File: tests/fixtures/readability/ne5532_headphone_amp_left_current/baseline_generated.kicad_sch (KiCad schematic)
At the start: 13 parts, among them J1 AudioIn_L, J2 AudioIn_R, J3 PowerSupply, J4 HeadphoneOut_L, J5 HeadphoneOut_R

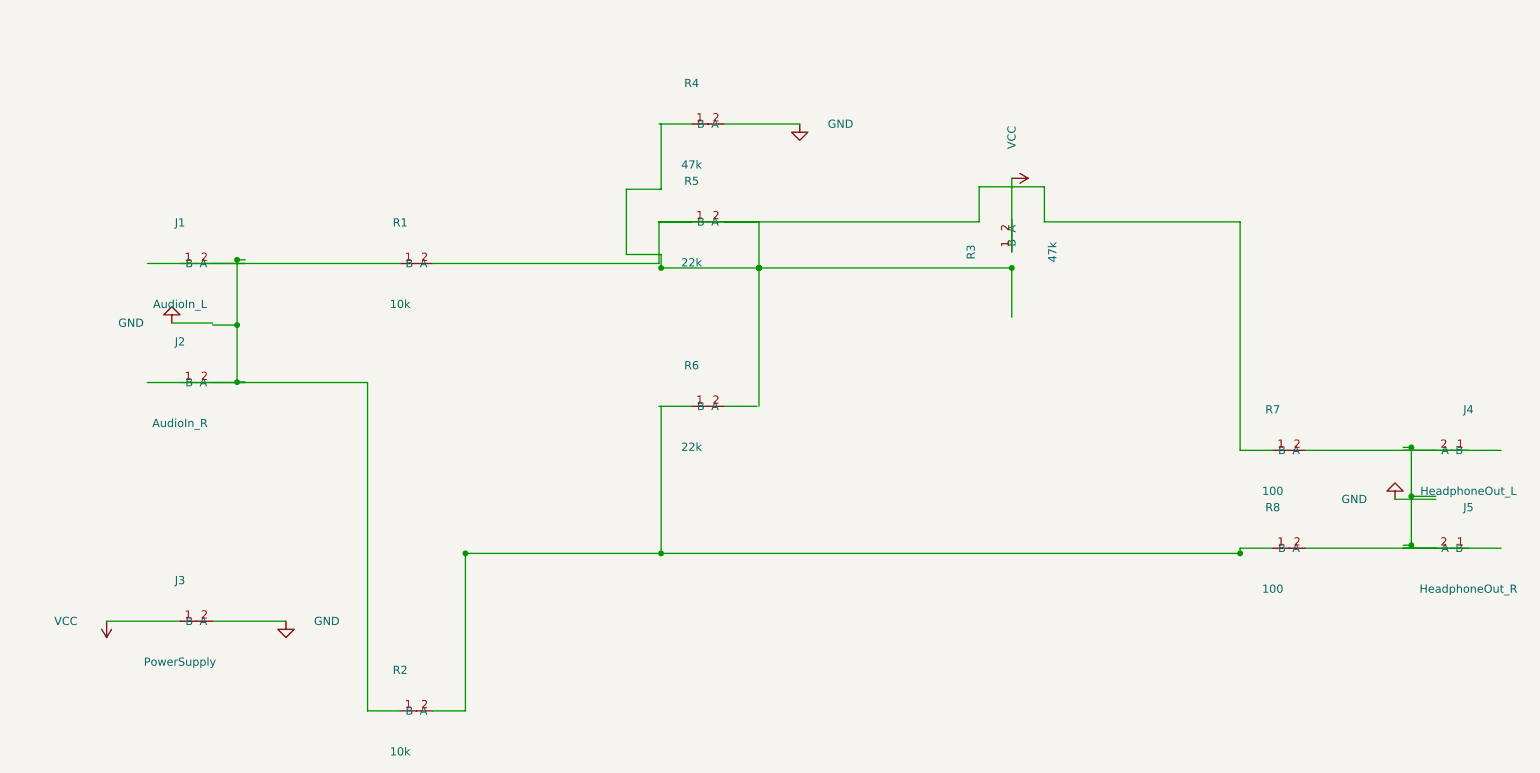
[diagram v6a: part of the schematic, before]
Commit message: fix: correct gnd symbol orientation
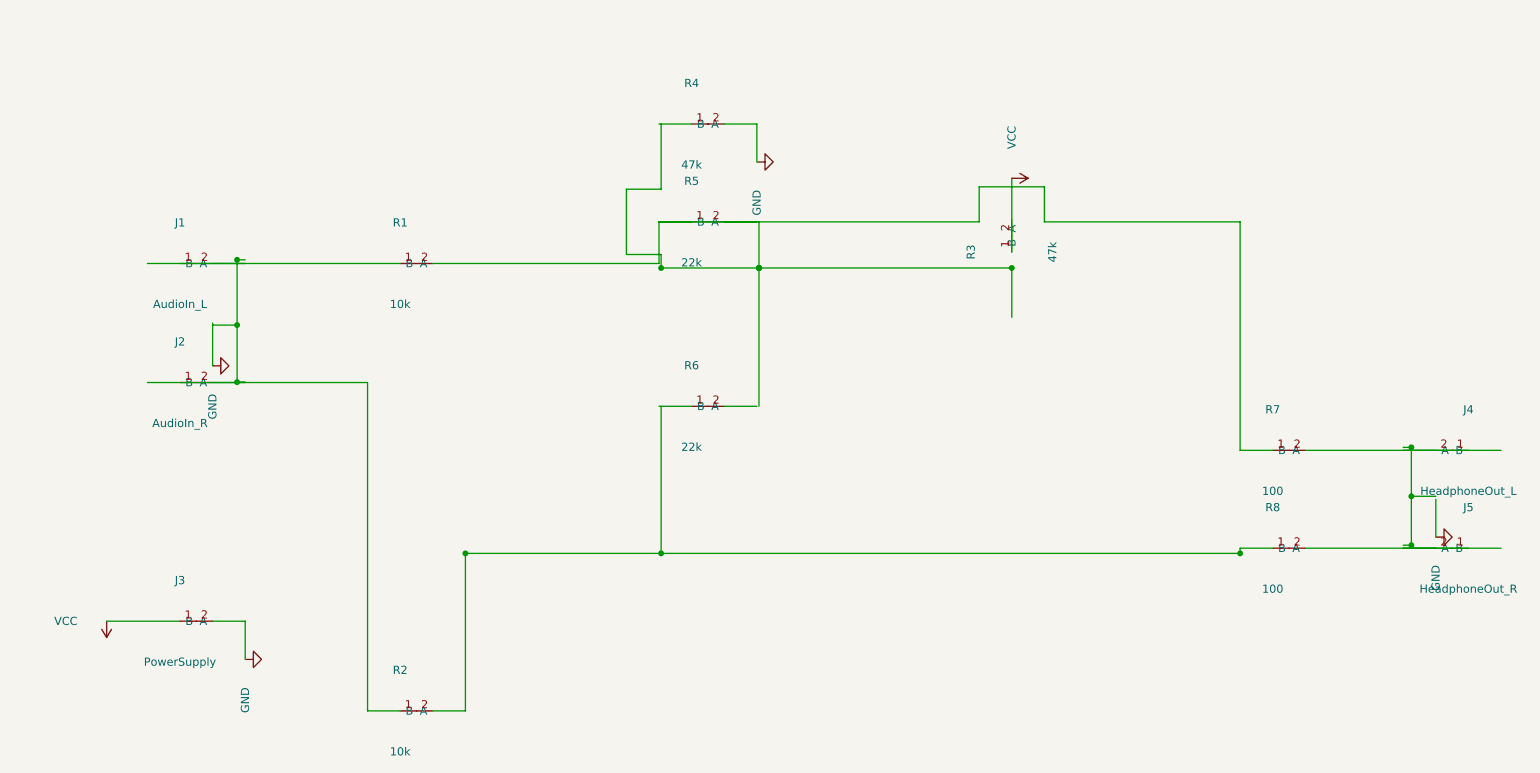
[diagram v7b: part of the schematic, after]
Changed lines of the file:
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@@
         "BaselineHeadphoneAmp"
         (path
-          "/0432db1b-1d3c-47e6-aa61-f27fe61c2f52/"
+          "/7582036d-d91e-40de-9a75-0636ee5f7de5/"
           (reference "J1")
           (unit 1)
@@
         "BaselineHeadphoneAmp"
         (path
-          "/0432db1b-1d3c-47e6-aa61-f27fe61c2f52/"
+          "/7582036d-d91e-40de-9a75-0636ee5f7de5/"
           (reference "J2")
           (unit 1)
@@
         "BaselineHeadphoneAmp"
         (path
-          "/0432db1b-1d3c-47e6-aa61-f27fe61c2f52/"
+          "/7582036d-d91e-40de-9a75-0636ee5f7de5/"
           (reference "J3")
           (unit 1)
@@
         "BaselineHeadphoneAmp"
         (path
-          "/0432db1b-1d3c-47e6-aa61-f27fe61c2f52/"
+          "/7582036d-d91e-40de-9a75-0636ee5f7de5/"
           (reference "J4")
           (unit 1)
@@
         "BaselineHeadphoneAmp"
         (path
-          "/0432db1b-1d3c-47e6-aa61-f27fe61c2f52/"
+          "/7582036d-d91e-40de-9a75-0636ee5f7de5/"
           (reference "J5")
           (unit 1)
@@
         "BaselineHeadphoneAmp"
         (path
-          "/0432db1b-1d3c-47e6-aa61-f27fe61c2f52/"
+          "/7582036d-d91e-40de-9a75-0636ee5f7de5/"
           (reference "R1")
           (unit 1)
@@
         "BaselineHeadphoneAmp"
         (path
-          "/0432db1b-1d3c-47e6-aa61-f27fe61c2f52/"
+          "/7582036d-d91e-40de-9a75-0636ee5f7de5/"
           (reference "R2")
           (unit 1)
@@
         "BaselineHeadphoneAmp"
         (path
-          "/0432db1b-1d3c-47e6-aa61-f27fe61c2f52/"
+          "/7582036d-d91e-40de-9a75-0636ee5f7de5/"
           (reference "R3")
           (unit 1)
@@
         "BaselineHeadphoneAmp"
         (path
-          "/0432db1b-1d3c-47e6-aa61-f27fe61c2f52/"
+          "/7582036d-d91e-40de-9a75-0636ee5f7de5/"
           (reference "R4")
           (unit 1)
@@
         "BaselineHeadphoneAmp"
         (path
-          "/0432db1b-1d3c-47e6-aa61-f27fe61c2f52/"
+          "/7582036d-d91e-40de-9a75-0636ee5f7de5/"
           (reference "R5")
           (unit 1)
@@
         "BaselineHeadphoneAmp"
         (path
-          "/0432db1b-1d3c-47e6-aa61-f27fe61c2f52/"
+          "/7582036d-d91e-40de-9a75-0636ee5f7de5/"
           (reference "R6")
           (unit 1)
@@
         "BaselineHeadphoneAmp"
         (path
-          "/0432db1b-1d3c-47e6-aa61-f27fe61c2f52/"
+          "/7582036d-d91e-40de-9a75-0636ee5f7de5/"
           (reference "R7")
           (unit 1)
@@
         "BaselineHeadphoneAmp"
         (path
-          "/0432db1b-1d3c-47e6-aa61-f27fe61c2f52/"
+          "/7582036d-d91e-40de-9a75-0636ee5f7de5/"
           (reference "R8")
           (unit 1)
@@
   )
   (wire
-    (pts (xy 55.88 108.90) (xy 49.53 108.90))
-    (stroke (width 0) (type default))
-  )
-  (wire
-    (pts (xy 55.88 155.34) (xy 67.31 155.34))
+    (pts (xy 55.88 108.90) (xy 55.88 115.57))
+    (stroke (width 0) (type default))
+  )
+  (wire
+    (pts (xy 55.88 155.34) (xy 60.96 155.34))
+    (stroke (width 0) (type default))
+  )
+  (wire
+    (pts (xy 60.96 155.34) (xy 60.96 161.29))
     (stroke (width 0) (type default))
   )
@@
   )
   (wire
-    (pts (xy 246.38 136.35) (xy 240.03 136.35))
-    (stroke (width 0) (type default))
-  )
-  (wire
-    (pts (xy 135.56 77.91) (xy 147.32 77.91))
+    (pts (xy 246.38 136.35) (xy 246.38 142.24))
+    (stroke (width 0) (type default))
+  )
+  (wire
+    (pts (xy 135.56 77.91) (xy 140.64 77.91))
+    (stroke (width 0) (type default))
+  )
+  (wire
+    (pts (xy 140.64 77.91) (xy 140.64 83.82))
     (stroke (width 0) (type default))
   )
@@
   (symbol
     (lib_id "power:GND")
-    (at 49.53 108.90 180)
+    (at 55.88 115.57 90)
     (unit 1)
     (exclude_from_sim yes)
@@
       "Reference"
       "#PWR01"
-      (at 49.53 108.90 0)
+      (at 55.88 115.57 0)
       (effects (font (size 1.27 1.27)) hide)
     )
@@
       "Value"
       "GND"
-      (at 43.18 108.90 0)
-      (effects (font (size 1.27 1.27)))
-    )
-    (property
-      "Footprint"
-      ""
-      (at 49.53 108.90 0)
-      (effects (font (size 1.27 1.27)) hide)
-    )
-    (property
-      "Datasheet"
-      "~"
-      (at 49.53 108.90 0)
-      (effects (font (size 1.27 1.27)) hide)
-    )
-    (pin "1")
-    (instances
-      (project
-        "BaselineHeadphoneAmp"
-        (path
-          "/0432db1b-1d3c-47e6-aa61-f27fe61c2f52/"
+      (at 55.88 121.92 0)
+      (effects (font (size 1.27 1.27)))
+    )
+    (property
+      "Footprint"
+      ""
+      (at 55.88 115.57 0)
+      (effects (font (size 1.27 1.27)) hide)
+    )
+    (property
+      "Datasheet"
+      "~"
+      (at 55.88 115.57 0)
+      (effects (font (size 1.27 1.27)) hide)
+    )
+    (pin "1")
+    (instances
+      (project
+        "BaselineHeadphoneAmp"
+        (path
+          "/7582036d-d91e-40de-9a75-0636ee5f7de5/"
           (reference "#PWR01")
           (unit 1)
@@
   (symbol
     (lib_id "power:GND")
-    (at 67.31 155.34 0)
+    (at 60.96 161.29 90)
     (unit 1)
     (exclude_from_sim yes)
@@
       "Reference"
       "#PWR02"
-      (at 67.31 155.34 0)
+      (at 60.96 161.29 0)
       (effects (font (size 1.27 1.27)) hide)
     )
@@
       "Value"
       "GND"
-      (at 73.66 155.34 0)
-      (effects (font (size 1.27 1.27)))
-    )
-    (property
-      "Footprint"
-      ""
-      (at 67.31 155.34 0)
-      (effects (font (size 1.27 1.27)) hide)
-    )
-    (property
-      "Datasheet"
-      "~"
-      (at 67.31 155.34 0)
-      (effects (font (size 1.27 1.27)) hide)
-    )
-    (pin "1")
-    (instances
-      (project
-        "BaselineHeadphoneAmp"
-        (path
-          "/0432db1b-1d3c-47e6-aa61-f27fe61c2f52/"
+      (at 60.96 167.64 0)
+      (effects (font (size 1.27 1.27)))
+    )
+    (property
+      "Footprint"
+      ""
+      (at 60.96 161.29 0)
+      (effects (font (size 1.27 1.27)) hide)
+    )
+    (property
+      "Datasheet"
+      "~"
+      (at 60.96 161.29 0)
+      (effects (font (size 1.27 1.27)) hide)
+    )
+    (pin "1")
+    (instances
+      (project
+        "BaselineHeadphoneAmp"
+        (path
+          "/7582036d-d91e-40de-9a75-0636ee5f7de5/"
           (reference "#PWR02")
           (unit 1)
@@
   (symbol
     (lib_id "power:GND")
-    (at 240.03 136.35 180)
+    (at 246.38 142.24 90)
     (unit 1)
     (exclude_from_sim yes)
@@
       "Reference"
       "#PWR03"
-      (at 240.03 136.35 0)
+      (at 246.38 142.24 0)
       (effects (font (size 1.27 1.27)) hide)
     )
@@
       "Value"
       "GND"
-      (at 233.68 136.35 0)
-      (effects (font (size 1.27 1.27)))
-    )
-    (property
-      "Footprint"
-      ""
-      (at 240.03 136.35 0)
-      (effects (font (size 1.27 1.27)) hide)
-    )
-    (property
-      "Datasheet"
-      "~"
-      (at 240.03 136.35 0)
-      (effects (font (size 1.27 1.27)) hide)
-    )
-    (pin "1")
-    (instances
-      (project
-        "BaselineHeadphoneAmp"
-        (path
-          "/0432db1b-1d3c-47e6-aa61-f27fe61c2f52/"
+      (at 246.38 148.59 0)
+      (effects (font (size 1.27 1.27)))
+    )
+    (property
+      "Footprint"
+      ""
+      (at 246.38 142.24 0)
+      (effects (font (size 1.27 1.27)) hide)
+    )
+    (property
+      "Datasheet"
+      "~"
+      (at 246.38 142.24 0)
+      (effects (font (size 1.27 1.27)) hide)
+    )
+    (pin "1")
+    (instances
+      (project
+        "BaselineHeadphoneAmp"
+        (path
+          "/7582036d-d91e-40de-9a75-0636ee5f7de5/"
           (reference "#PWR03")
           (unit 1)
@@
   (symbol
     (lib_id "power:GND")
-    (at 147.32 77.91 0)
+    (at 140.64 83.82 90)
     (unit 1)
     (exclude_from_sim yes)
@@
       "Reference"
       "#PWR04"
-      (at 147.32 77.91 0)
+      (at 140.64 83.82 0)
       (effects (font (size 1.27 1.27)) hide)
     )
@@
       "Value"
       "GND"
-      (at 153.67 77.91 0)
-      (effects (font (size 1.27 1.27)))
-    )
-    (property
-      "Footprint"
-      ""
-      (at 147.32 77.91 0)
-      (effects (font (size 1.27 1.27)) hide)
-    )
-    (property
-      "Datasheet"
-      "~"
-      (at 147.32 77.91 0)
-      (effects (font (size 1.27 1.27)) hide)
-    )
-    (pin "1")
-    (instances
-      (project
-        "BaselineHeadphoneAmp"
-        (path
-          "/0432db1b-1d3c-47e6-aa61-f27fe61c2f52/"
+      (at 140.64 90.17 0)
+      (effects (font (size 1.27 1.27)))
+    )
+    (property
+      "Footprint"
+      ""
+      (at 140.64 83.82 0)
+      (effects (font (size 1.27 1.27)) hide)
+    )
+    (property
+      "Datasheet"
+      "~"
+      (at 140.64 83.82 0)
+      (effects (font (size 1.27 1.27)) hide)
+    )
+    (pin "1")
+    (instances
+      (project
+        "BaselineHeadphoneAmp"
+        (path
+          "/7582036d-d91e-40de-9a75-0636ee5f7de5/"
           (reference "#PWR04")
           (unit 1)
@@
         "BaselineHeadphoneAmp"
         (path
-          "/0432db1b-1d3c-47e6-aa61-f27fe61c2f52/"
+          "/7582036d-d91e-40de-9a75-0636ee5f7de5/"
           (reference "#PWR05")
           (unit 1)
@@
         "BaselineHeadphoneAmp"
         (path
-          "/0432db1b-1d3c-47e6-aa61-f27fe61c2f52/"
+          "/7582036d-d91e-40de-9a75-0636ee5f7de5/"
           (reference "#PWR06")
           (unit 1)
@@
     (effects (font (size 1.27 1.27)) (justify left) hide)
   )
-  (sheet_instances (path "/0432db1b-1d3c-47e6-aa61-f27fe61c2f52/" (page "1")))
+  (sheet_instances (path "/7582036d-d91e-40de-9a75-0636ee5f7de5/" (page "1")))
 )
